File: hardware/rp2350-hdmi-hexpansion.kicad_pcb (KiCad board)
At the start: 4 copper layers, 47.3 x 54.3 mm, 58 parts, among them J1 Hexpansion-Connector, J3 SWD, J4 Qwiic, J5 HDMI-A, SW3 RESET, U1 RP2354A, U4 TPS61023DRLR, U6 TPD4E05U06, U7 TPD4E05U06, Y1 12MHz

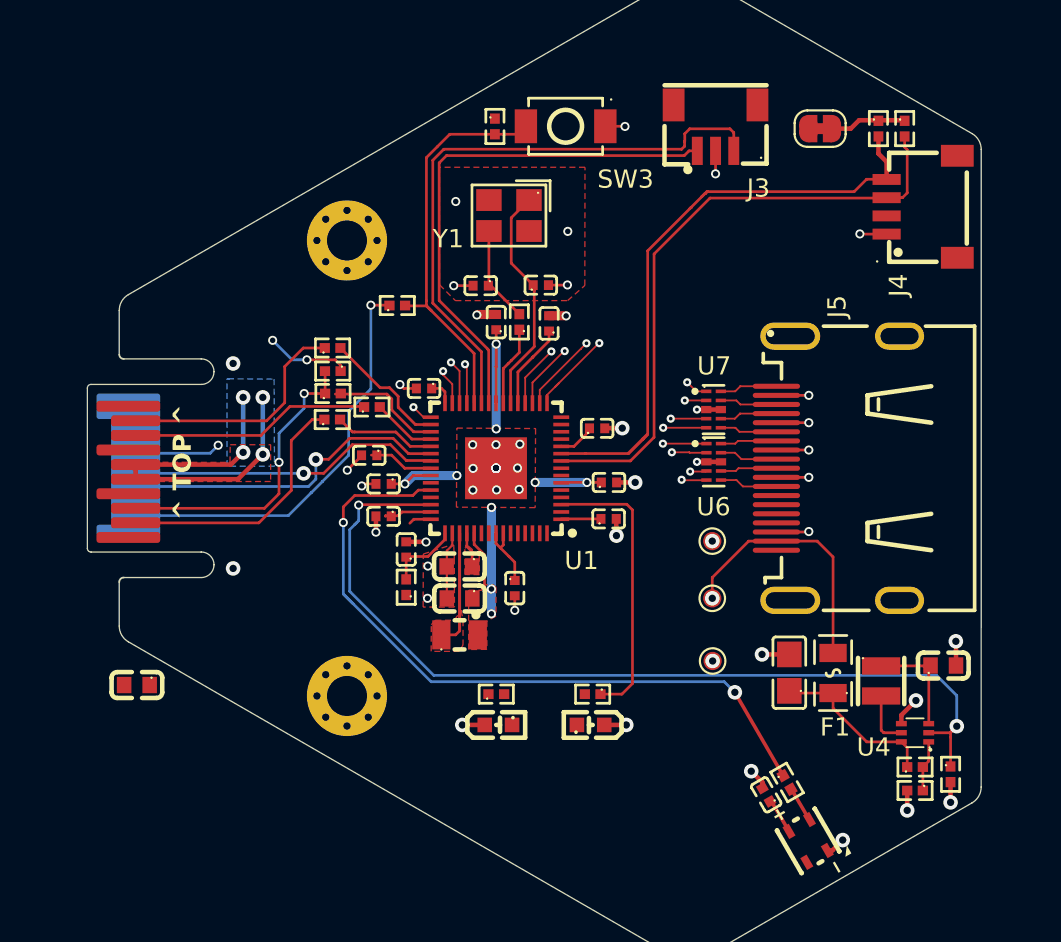
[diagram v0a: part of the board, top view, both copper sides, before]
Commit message: hardware: finish HDMI routing, clear C14 clearance, DRC exclusions
Co-Authored-By: Claude Sonnet 5.5 <noreply@anthropic.com>
Claude-Session: https://claude.ai/code/session_01VMD2iSg4JfioYFvgvvdo7j
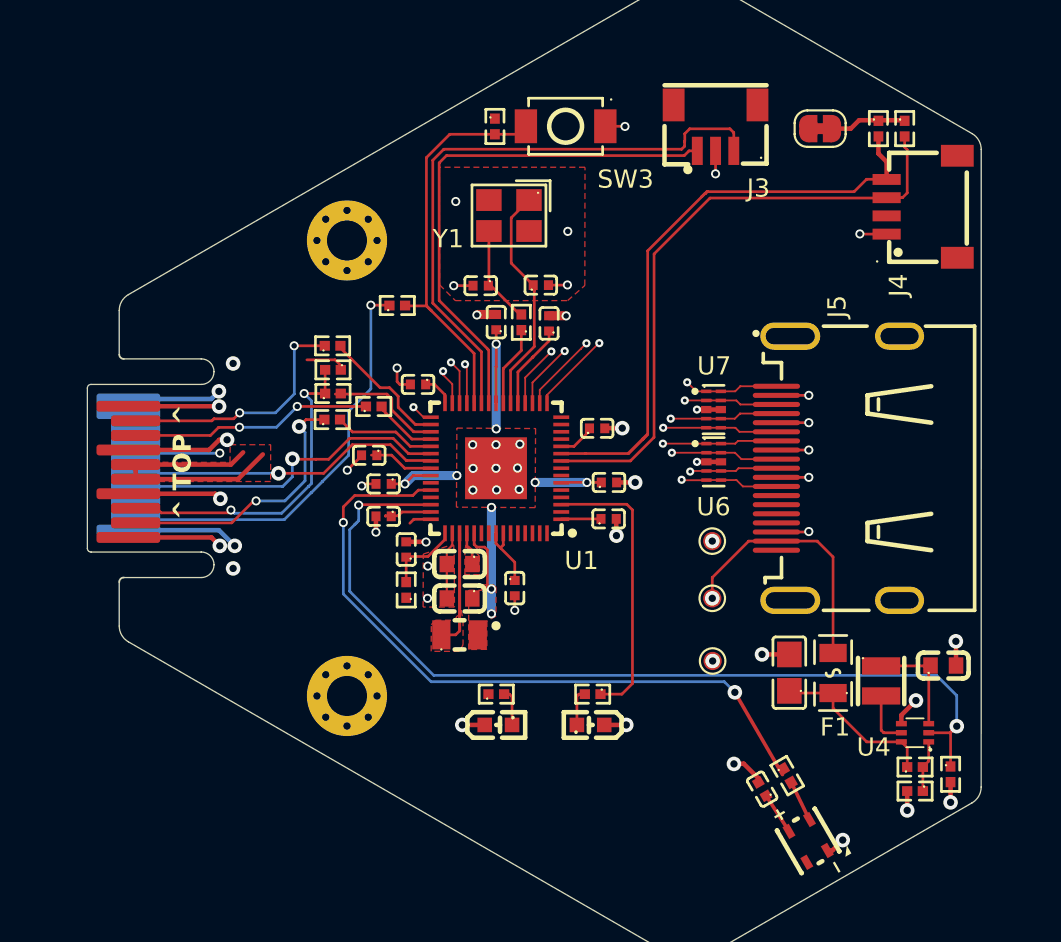
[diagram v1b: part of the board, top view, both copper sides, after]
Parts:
- removed C16: 10uF, jlc:C0603
- moved C6 0.40 mm to (116.4, 95.4)
- moved C32 0.38 mm to (135.3, 117.6)
- moved R52 0.38 mm to (136.7, 116.9)
- moved R1 0.15 mm to (115.8, 106.7)
- moved C14 0.13 mm to (118.7, 105.3)
- moved R36 0.12 mm to (111.7, 93.3)
- moved R2 0.11 mm to (122.1, 92.0)
- moved R38 0.10 mm to (114.0, 96.6)
- moved R41 0.07 mm to (111.7, 94.6)
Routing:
- net GND: track 48.0 -> 81.2 mm, vias 59 -> 55
- net +3V3: track 54.6 -> 46.1 mm, vias 7 -> 1
- net /LED2_A: track 0.00 -> 2.06 mm
- net /LED1_A: track 0.00 -> 2.04 mm
- net /HDMI_D2_N: track 15.8 -> 16.9 mm
- net /HDMI_D0_P: track 22.6 -> 23.4 mm
- net /HDMI_D0_N: track 23.9 -> 24.7 mm
- net /HDMI_D1_P: track 20.7 -> 21.5 mm
- net /HDMI_D1_N: track 22.1 -> 22.9 mm
- net /HDMI_CK_P: track 19.5 -> 20.3 mm
- net /HDMI_CK_N: track 20.6 -> 21.4 mm
- net /RGB_DIN: track 34.4 -> 33.7 mm
- net /RUN: track 22.2 -> 21.5 mm
- net /HS_F: track 13.2 -> 13.8 mm, vias 0 -> 2
- net /HDMI_D2_P: track 14.9 -> 15.4 mm
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- removed copper zone on B.Cu, net +3V3
